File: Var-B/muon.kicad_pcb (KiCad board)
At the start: 2 copper layers, 20 x 13 mm, 9 parts, among them J1 HRO_TYPE-C-31-M-12, J2 SM04B-SRSS-TB, U1 TPD4E05U06DQA

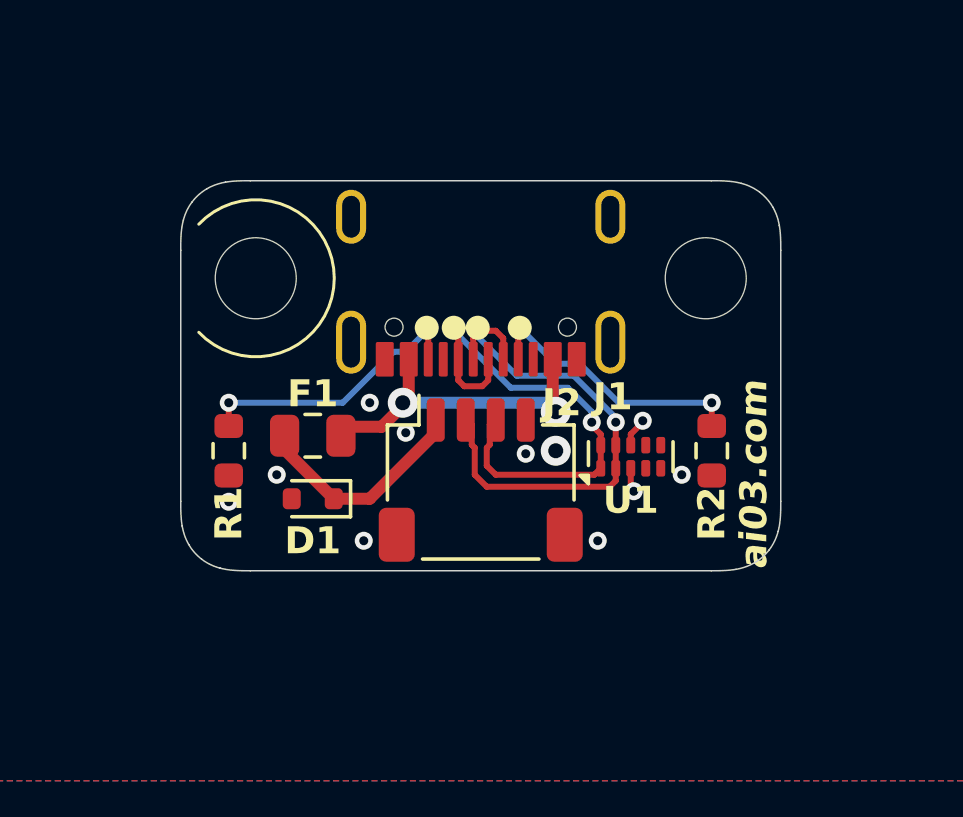
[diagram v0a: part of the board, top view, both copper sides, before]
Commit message: Update B variant to B2
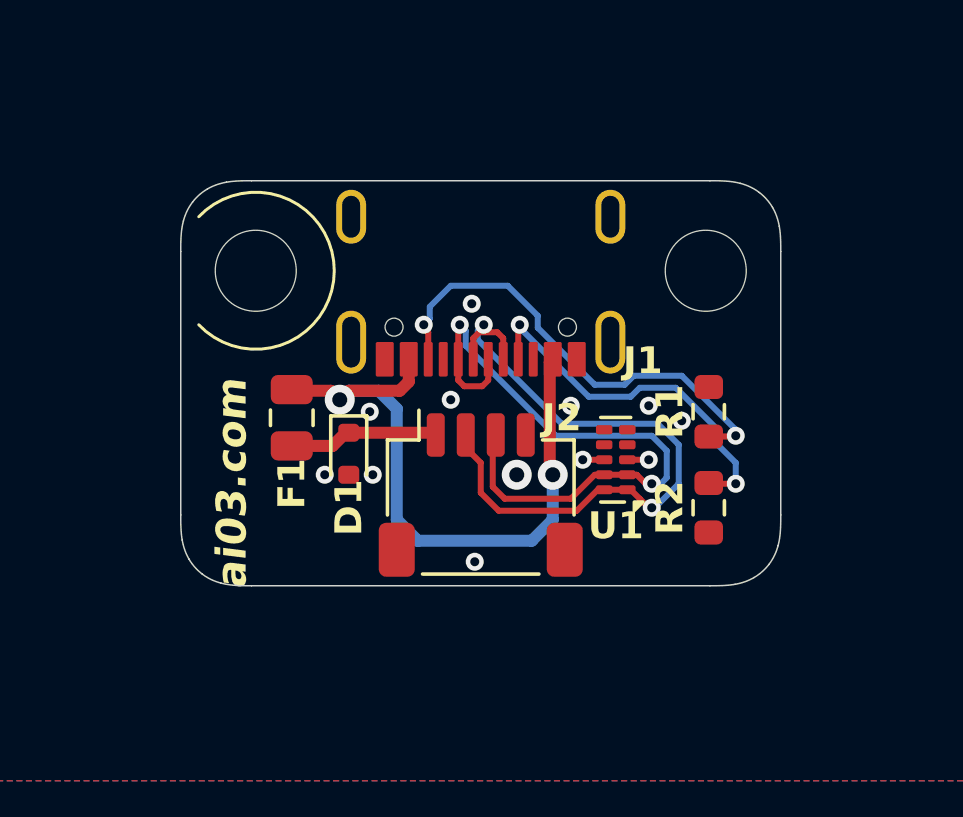
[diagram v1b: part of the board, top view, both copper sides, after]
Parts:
- moved R1 16.1 mm to (81.6, 57.7), turned to 90 degrees
- moved D1 1.92 mm to (69.6, 59.1), turned to -90 degrees
- moved R2 1.90 mm to (81.6, 60.9)
- moved F1 0.92 mm to (67.7, 57.9), turned to -90 degrees
- moved U1 0.51 mm to (78.5, 59.3), turned to 180 degrees
- moved J2 0.50 mm to (74.0, 60.4)
- moved MH1 0.25 mm to (81.5, 53.0)
- moved MH2 0.25 mm to (66.5, 53.0)
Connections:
- net Net-(J1-CC1) renamed CC1
- net Net-(J1-CC2) renamed CC2
- U1 pad 1: D+ -> D-
- U1 pad 2: D- -> D+
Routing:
- net VBUS: track 11.1 -> 22.2 mm
- net CC2: track 9.69 -> 16.0 mm
- net D+: track 17.1 -> 21.8 mm
- net D-: track 18.1 -> 22.8 mm
- net CC1: track 9.43 -> 12.5 mm
- net +5V: track 7.56 -> 5.01 mm
- net GND: track 1.79 -> 1.43 mm, vias 11 -> 12
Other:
- board size 20 x 13 mm -> 20 x 13.5 mm
- board text added: "B2"
- board text removed: "B1"
